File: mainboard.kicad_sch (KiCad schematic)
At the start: 86 parts, among them J1 Conn 02x05 1.27mm, J2 Conn 01x10 1.27mm, J3 Conn 02x10 1.27mm, J4 Conn +Z 02x05 2.00 mm, J5 Conn -Z 02x05 2.00 mm, J6 Conn +X 02x05 2.00 mm, J7 Conn -X 02x05 2.00 mm, J8 U.FL-R-SMT-1, J9 USB_C_Receptacle_USB2.0, SW1 KMR231NG, SW2 SW_SPDT, U1 ATSAMD51J20A-M, U10 USBLC6-2SC6, U2 MAX706RESA+, U3 AP2112K-3.3, U4 MR25H40, U5 BMX160, U6 RFM98PW, U7 DRV8830DRC, U8 DRV8830DRC, U9 DRV8830DRC, Y1 32.768kHz

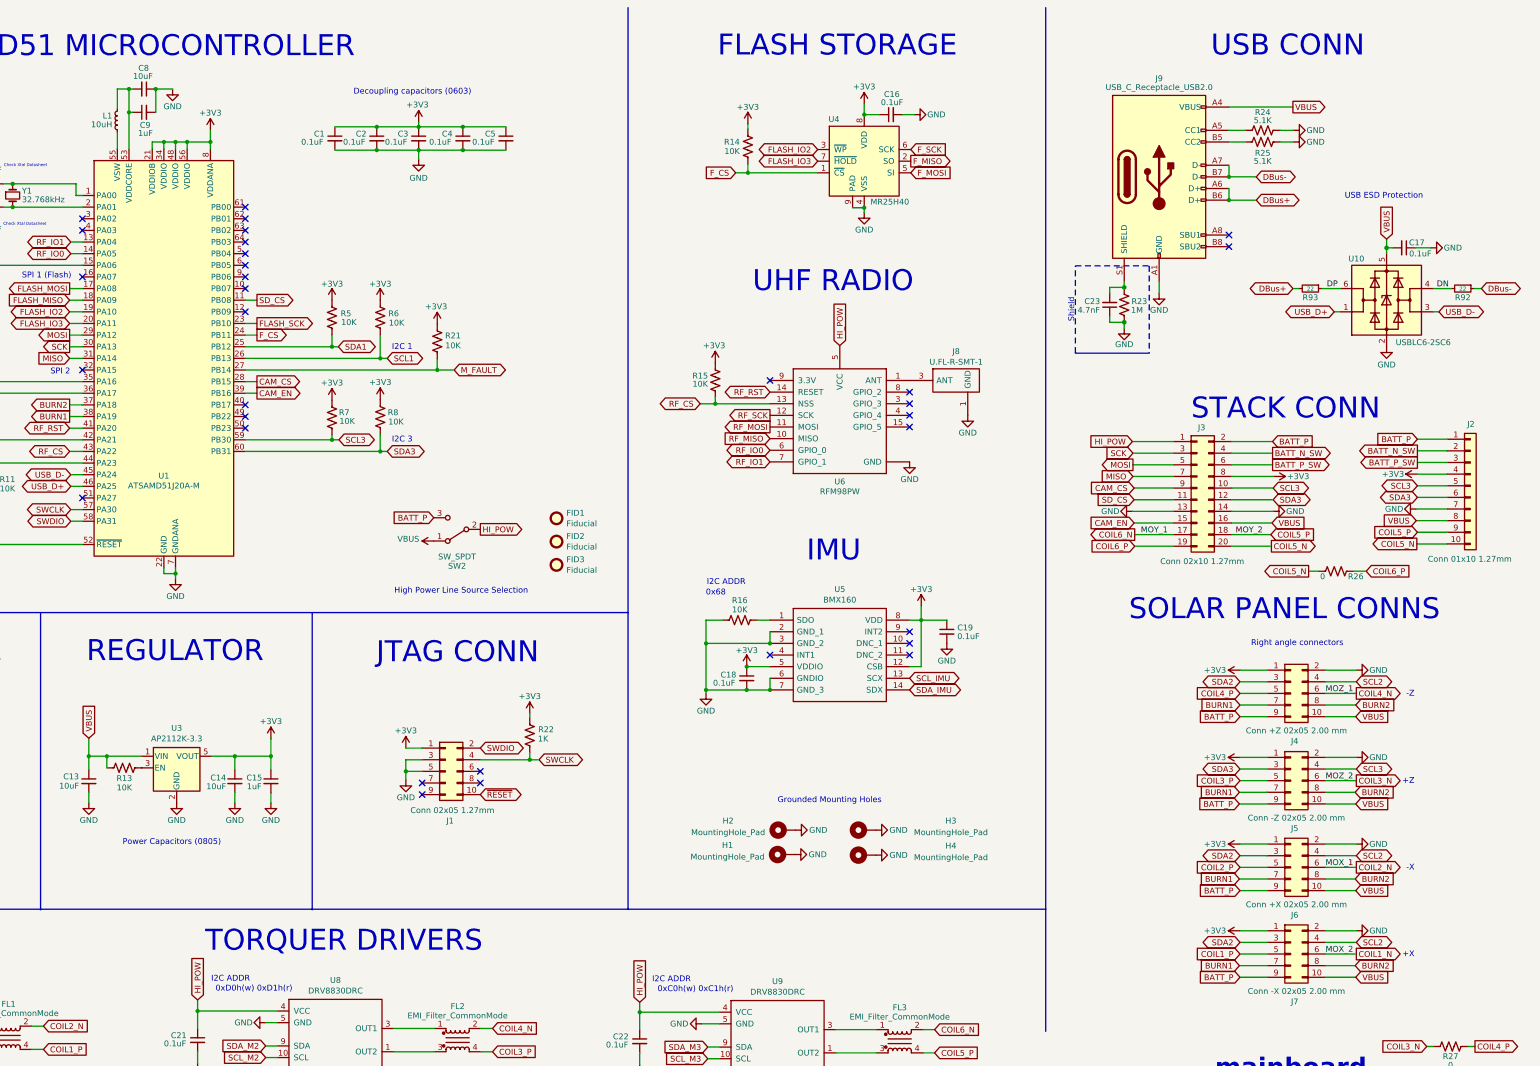
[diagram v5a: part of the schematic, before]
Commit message: added pulldown and 0 ohm resistor to VBUS. Renamed VBUS to VUSB
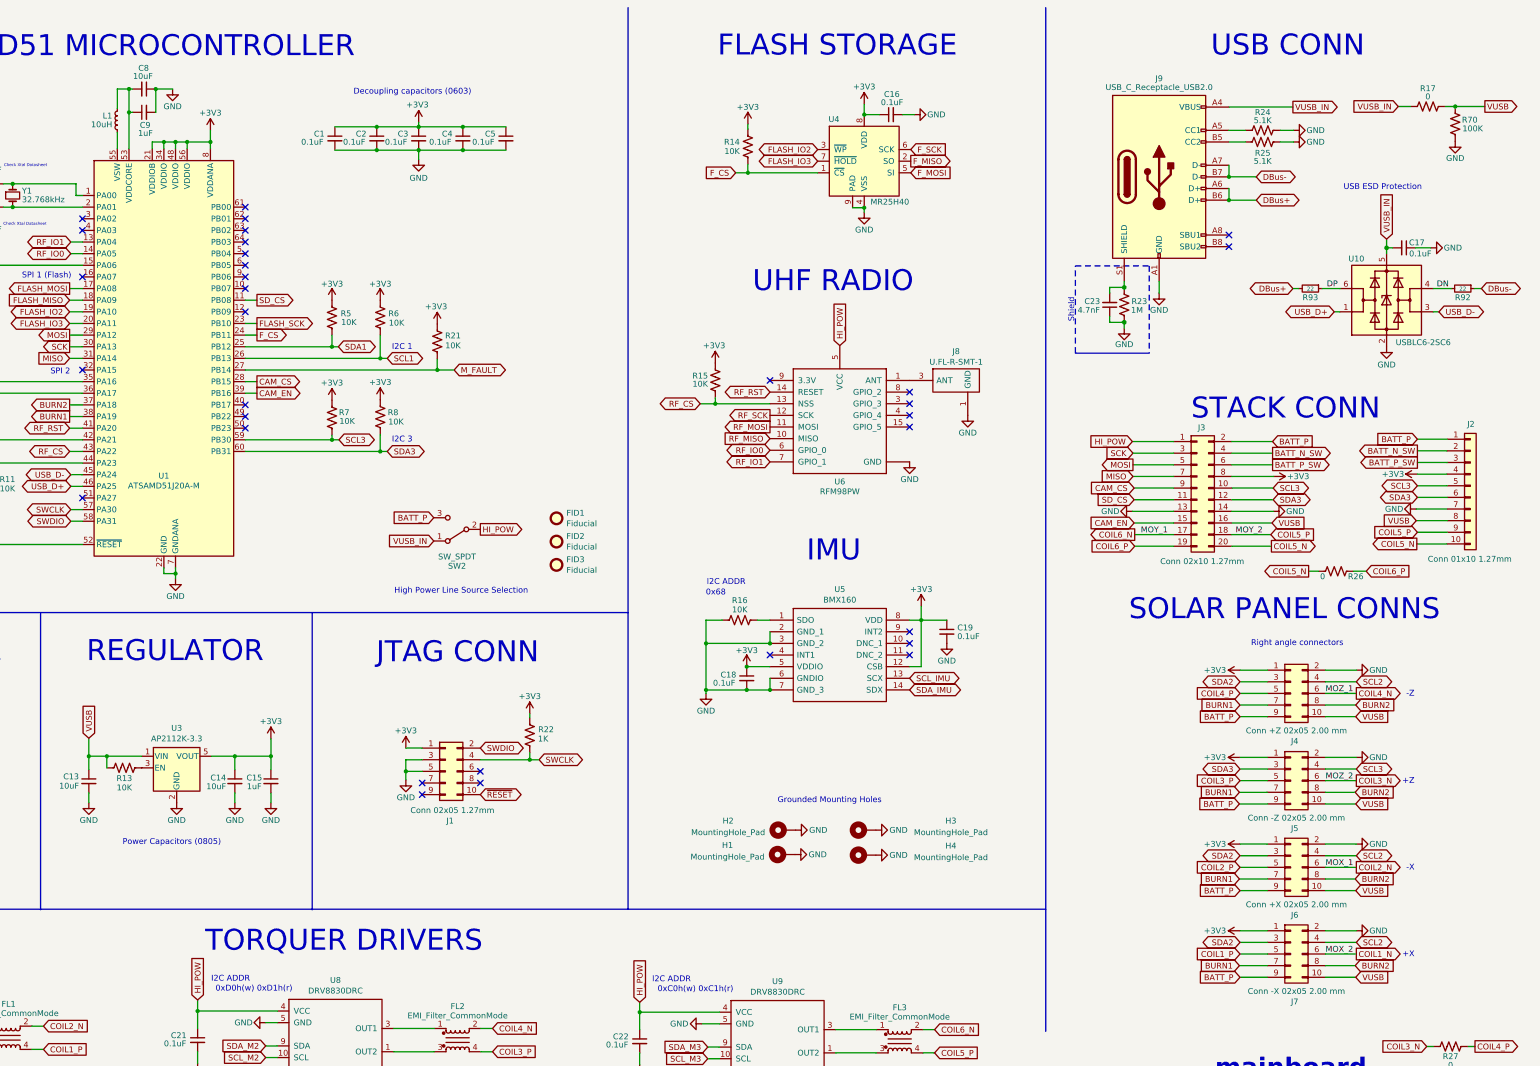
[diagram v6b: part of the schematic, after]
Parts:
- added R17: 0, Resistor_SMD:R_0603_1608Metric, symbol Device:R_US
- added R70: 100K, Resistor_SMD:R_0603_1608Metric, symbol Device:R_US
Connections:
- net GND: now also R70.2
- net VBUS renamed VUSB
- net VUSB: now also R17.2, R70.1; no longer C17.2, J9.A4 (VBUS), J9.A9 (VBUS), J9.B4 (VBUS), J9.B9 (VBUS), SW2.1 (A), U10.5 (VBUS)
- new net VUSB_IN: C17.2, J9.A4 (VBUS), J9.A9 (VBUS), J9.B4 (VBUS), J9.B9 (VBUS), R17.1, SW2.1 (A), U10.5 (VBUS)
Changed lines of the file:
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@@
   (junction (at 56.261 129.159) (diameter 0) (color 0 0 0 0)
   )
+  (junction (at 401.32 33.528) (diameter 0) (color 0 0 0 0)
+  )
   (junction (at 329.057 73.025) (diameter 1.016) (color 0 0 0 0)
   )
@@
     (stroke (width 0) (type default) (color 0 0 0 0))
   )
+  (wire (pts (xy 401.32 33.528) (xy 407.797 33.528))
+    (stroke (width 0) (type default) (color 0 0 0 0))
+  )
   (wire (pts (xy 144.145 233.553) (xy 141.605 233.553))
     (stroke (width 0) (type default) (color 0 0 0 0))
@@
     (stroke (width 0) (type default) (color 0 0 0 0))
   )
+  (wire (pts (xy 388.874 33.528) (xy 391.541 33.528))
+    (stroke (width 0) (type default) (color 0 0 0 0))
+  )
   (wire (pts (xy 139.7 96.139) (xy 137.16 96.139))
     (stroke (width 0) (type default) (color 0 0 0 0))
@@
     (stroke (width 0) (type default) (color 0 0 0 0))
   )
+  (wire (pts (xy 401.32 33.528) (xy 399.161 33.528))
+    (stroke (width 0) (type default) (color 0 0 0 0))
+  )
   (wire (pts (xy 46.101 248.285) (xy 43.561 248.285))
     (stroke (width 0) (type default) (color 0 0 0 0))
@@
     (effects (font (size 1.27 1.27)) (justify right bottom))
   )
-  (text "USB ESD Protection" (at 377.19 53.848 0)
+  (text "USB ESD Protection" (at 376.936 51.943 0)
     (effects (font (size 1.27 1.27)) (justify left bottom))
   )
@@
     )
   )
-  (global_label "VBUS" (shape input) (at 102.997 171.45 90) (fields_autoplaced)
+  (global_label "VUSB" (shape input) (at 102.997 171.45 90) (fields_autoplaced)
     (effects (font (size 1.27 1.27)) (justify left))
     (property "Intersheet References" "${INTERSHEET_REFS}" (id 0) (at 102.9176 164.2272 90)
@@
     )
   )
+  (global_label "VUSB_IN" (shape input) (at 388.874 33.528 180) (fields_autoplaced)
+    (effects (font (size 1.27 1.27)) (justify right))
+    (property "Intersheet References" "${INTERSHEET_REFS}" (id 0) (at 378.7484 33.6074 0)
+      (effects (font (size 1.27 1.27)) (justify right) hide)
+    )
+  )
   (global_label "DBus-" (shape bidirectional) (at 357.886 48.895 0) (fields_autoplaced)
     (effects (font (size 1.27 1.27)) (justify left))
@@
     )
   )
-  (global_label "VBUS" (shape input) (at 379.603 185.801 0) (fields_autoplaced)
+  (global_label "VUSB" (shape input) (at 379.603 185.801 0) (fields_autoplaced)
     (effects (font (size 1.27 1.27)) (justify left))
     (property "Intersheet References" "${INTERSHEET_REFS}" (id 0) (at 386.8258 185.7216 0)
@@
     )
   )
-  (global_label "VBUS" (shape input) (at 392.811 123.952 180) (fields_autoplaced)
+  (global_label "VUSB" (shape input) (at 392.811 123.952 180) (fields_autoplaced)
     (effects (font (size 1.27 1.27)) (justify right))
     (property "Intersheet References" "${INTERSHEET_REFS}" (id 0) (at 385.5882 124.0314 0)
@@
     )
   )
+  (global_label "VUSB" (shape output) (at 407.797 33.528 0) (fields_autoplaced)
+    (effects (font (size 1.27 1.27)) (justify left))
+    (property "Intersheet References" "${INTERSHEET_REFS}" (id 0) (at 415.0198 33.4486 0)
+      (effects (font (size 1.27 1.27)) (justify left) hide)
+    )
+  )
   (global_label "COIL6_P" (shape input) (at 331.343 129.54 180) (fields_autoplaced)
     (effects (font (size 1.27 1.27)) (justify right))
@@
     )
   )
+  (global_label "VUSB_IN" (shape input) (at 178.308 128.397 180) (fields_autoplaced)
+    (effects (font (size 1.27 1.27)) (justify right))
+    (property "Intersheet References" "${INTERSHEET_REFS}" (id 0) (at 168.1824 128.4764 0)
+      (effects (font (size 1.27 1.27)) (justify right) hide)
+    )
+  )
   (global_label "COIL5_P" (shape input) (at 287.655 240.157 0) (fields_autoplaced)
     (effects (font (size 1.27 1.27)) (justify left))
@@
     )
   )
-  (global_label "VBUS" (shape output) (at 365.887 33.655 0) (fields_autoplaced)
+  (global_label "VUSB_IN" (shape output) (at 365.887 33.655 0) (fields_autoplaced)
     (effects (font (size 1.27 1.27)) (justify left))
-    (property "Intersheet References" "${INTERSHEET_REFS}" (id 0) (at 373.1098 33.5756 0)
+    (property "Intersheet References" "${INTERSHEET_REFS}" (id 0) (at 376.0126 33.5756 0)
       (effects (font (size 1.27 1.27)) (justify left) hide)
     )
@@
     )
   )
-  (global_label "VBUS" (shape input) (at 379.603 223.647 0) (fields_autoplaced)
+  (global_label "VUSB" (shape input) (at 379.603 223.647 0) (fields_autoplaced)
     (effects (font (size 1.27 1.27)) (justify left))
     (property "Intersheet References" "${INTERSHEET_REFS}" (id 0) (at 386.8258 223.5676 0)
@@
     )
   )
-  (global_label "VBUS" (shape input) (at 379.603 166.751 0) (fields_autoplaced)
+  (global_label "VUSB" (shape input) (at 379.603 166.751 0) (fields_autoplaced)
     (effects (font (size 1.27 1.27)) (justify left))
     (property "Intersheet References" "${INTERSHEET_REFS}" (id 0) (at 386.8258 166.6716 0)
@@
     )
   )
-  (global_label "VBUS" (shape input) (at 379.603 204.724 0) (fields_autoplaced)
+  (global_label "VUSB" (shape input) (at 379.603 204.724 0) (fields_autoplaced)
     (effects (font (size 1.27 1.27)) (justify left))
     (property "Intersheet References" "${INTERSHEET_REFS}" (id 0) (at 386.8258 204.6446 0)
@@
     )
   )
-  (global_label "VBUS" (shape input) (at 361.315 124.46 0) (fields_autoplaced)
+  (global_label "VUSB" (shape input) (at 361.315 124.46 0) (fields_autoplaced)
     (effects (font (size 1.27 1.27)) (justify left))
     (property "Intersheet References" "${INTERSHEET_REFS}" (id 0) (at 368.5378 124.5394 0)
@@
     )
   )
-  (global_label "VBUS" (shape input) (at 386.334 62.484 90) (fields_autoplaced)
+  (global_label "VUSB_IN" (shape input) (at 386.334 62.484 90) (fields_autoplaced)
     (effects (font (size 1.27 1.27)) (justify left))
-    (property "Intersheet References" "${INTERSHEET_REFS}" (id 0) (at 386.2546 55.2612 90)
+    (property "Intersheet References" "${INTERSHEET_REFS}" (id 0) (at 386.2546 52.3584 90)
       (effects (font (size 1.27 1.27)) (justify left) hide)
     )
@@
     (pin "2")
   )
+  (symbol (lib_id "Device:R_US") (at 395.351 33.528 90) (unit 1)
+    (in_bom yes) (on_board yes)
+    (property "Reference" "R17" (id 0) (at 395.351 29.591 90))
+    (property "Value" "0" (id 1) (at 395.351 31.369 90))
+    (property "Footprint" "Resistor_SMD:R_0603_1608Metric" (id 2) (at 395.605 32.512 90)
+      (effects (font (size 1.27 1.27)) hide)
+    )
+    (property "Datasheet" "~" (id 3) (at 395.351 33.528 0)
+      (effects (font (size 1.27 1.27)) hide)
+    )
+    (pin "1")
+    (pin "2")
+  )
   (symbol (lib_id "power:GND") (at 274.828 191.516 90) (unit 1)
     (in_bom yes) (on_board yes)
@@
     (pin "2")
   )
+  (symbol (lib_id "Device:R_US") (at 401.32 37.338 0) (unit 1)
+    (in_bom yes) (on_board yes)
+    (property "Reference" "R70" (id 0) (at 404.495 36.449 0))
+    (property "Value" "100K" (id 1) (at 405.13 38.354 0))
+    (property "Footprint" "Resistor_SMD:R_0603_1608Metric" (id 2) (at 402.336 37.592 90)
+      (effects (font (size 1.27 1.27)) hide)
+    )
+    (property "Datasheet" "~" (id 3) (at 401.32 37.338 0)
+      (effects (font (size 1.27 1.27)) hide)
+    )
+    (pin "1")
+    (pin "2")
+  )
   (symbol (lib_id "power:GND") (at 395.986 64.389 90) (unit 1)
     (in_bom yes) (on_board yes)
@@
     (pin "1")
   )
+  (symbol (lib_id "power:GND") (at 401.32 41.148 0) (unit 1)
+    (in_bom yes) (on_board yes)
+    (property "Reference" "#PWR0124" (id 0) (at 401.32 47.498 0)
+      (effects (font (size 1.27 1.27)) hide)
+    )
+    (property "Value" "GND" (id 1) (at 401.32 44.831 0))
+    (property "Footprint" "" (id 2) (at 401.32 41.148 0)
+      (effects (font (size 1.27 1.27)) hide)
+    )
+    (property "Datasheet" "" (id 3) (at 401.32 41.148 0)
+      (effects (font (size 1.27 1.27)) hide)
+    )
+    (pin "1")
+  )
   (symbol (lib_id "power:GND") (at 329.057 81.915 0) (unit 1)
     (in_bom yes) (on_board yes)
@@
     (pin "2")
   )
-  (symbol (lib_id "power:VBUS") (at 178.308 128.397 90) (unit 1)
-    (in_bom yes) (on_board yes) (fields_autoplaced)
-    (property "Reference" "#PWR0112" (id 0) (at 182.118 128.397 0)
-      (effects (font (size 1.27 1.27)) hide)
-    )
-    (property "Value" "VBUS" (id 1) (at 175.133 127.9632 90)
-      (effects (font (size 1.27 1.27)) (justify left))
-    )
-    (property "Footprint" "" (id 2) (at 178.308 128.397 0)
-      (effects (font (size 1.27 1.27)) hide)
-    )
-    (property "Datasheet" "" (id 3) (at 178.308 128.397 0)
-      (effects (font (size 1.27 1.27)) hide)
-    )
-    (pin "1")
-  )
   (symbol (lib_id "Device:C_Small") (at 175.006 40.513 0) (unit 1)
     (in_bom yes) (on_board yes)
@@
       (reference "#PWR0111") (unit 1) (value "GND") (footprint "")
     )
-    (path "/dace08e9-2794-4eeb-968a-8ff63b4b9f51"
-      (reference "#PWR0112") (unit 1) (value "VBUS") (footprint "")
-    )
     (path "/2e088d9c-4345-4234-9fbc-b28bd25e7d74"
       (reference "#PWR0113") (unit 1) (value "+3V3") (footprint "")
@@
       (reference "#PWR0123") (unit 1) (value "GND") (footprint "")
     )
+    (path "/50e5377b-5519-48e6-ba4e-974f66fffe95"
+      (reference "#PWR0124") (unit 1) (value "GND") (footprint "")
+    )
     (path "/cd60d17a-4ffb-4042-a426-fdeb8e7d577a"
       (reference "#PWR0126") (unit 1) (value "+3V3") (footprint "")
@@
       (reference "R16") (unit 1) (value "10K") (footprint "Resistor_SMD:R_0603_1608Metric")
     )
+    (path "/1d7e6e2e-67a0-4278-a837-5da214f06a1e"
+      (reference "R17") (unit 1) (value "0") (footprint "Resistor_SMD:R_0603_1608Metric")
+    )
     (path "/00000000-0000-0000-0000-00005e74913a"
       (reference "R18") (unit 1) (value "0") (footprint "Resistor_SMD:R_0603_1608Metric")
@@
       (reference "R69") (unit 1) (value "0") (footprint "Resistor_SMD:R_0603_1608Metric")
     )
+    (path "/44714030-b74c-47b1-8cdb-296d3c08673a"
+      (reference "R70") (unit 1) (value "100K") (footprint "Resistor_SMD:R_0603_1608Metric")
+    )
     (path "/89e9ad27-deb2-49f4-bcf8-1a7a63ce9e3a/d08973d1-a9aa-4e3b-a55a-a663d36864d8"

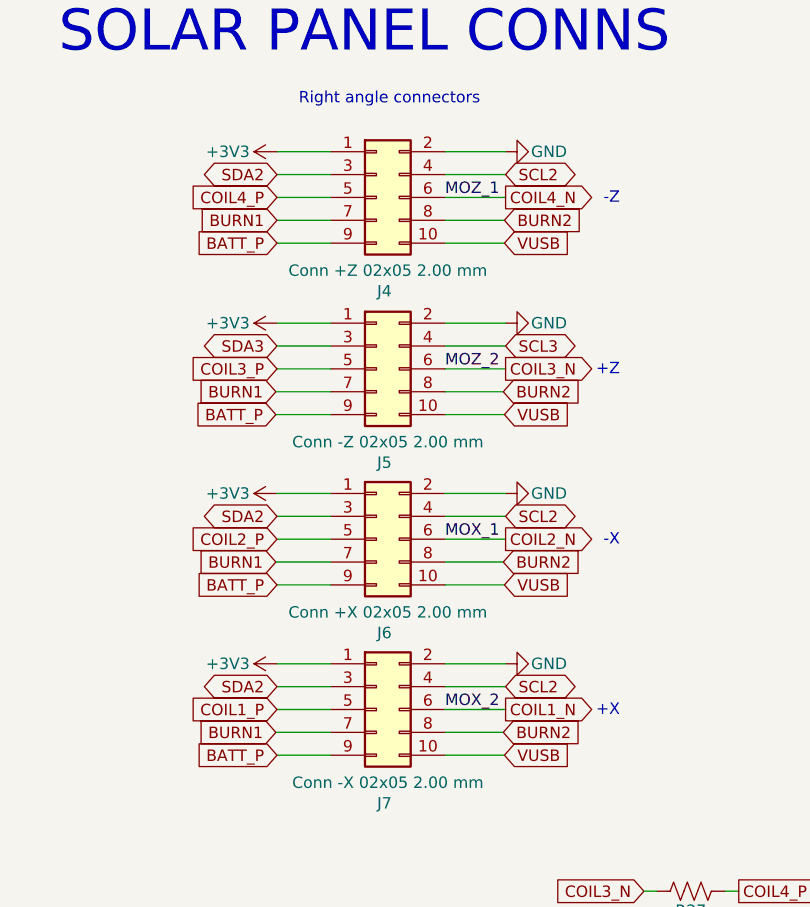
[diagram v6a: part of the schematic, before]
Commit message: Updated Mainboard-Solar Panels X/Z Connectors
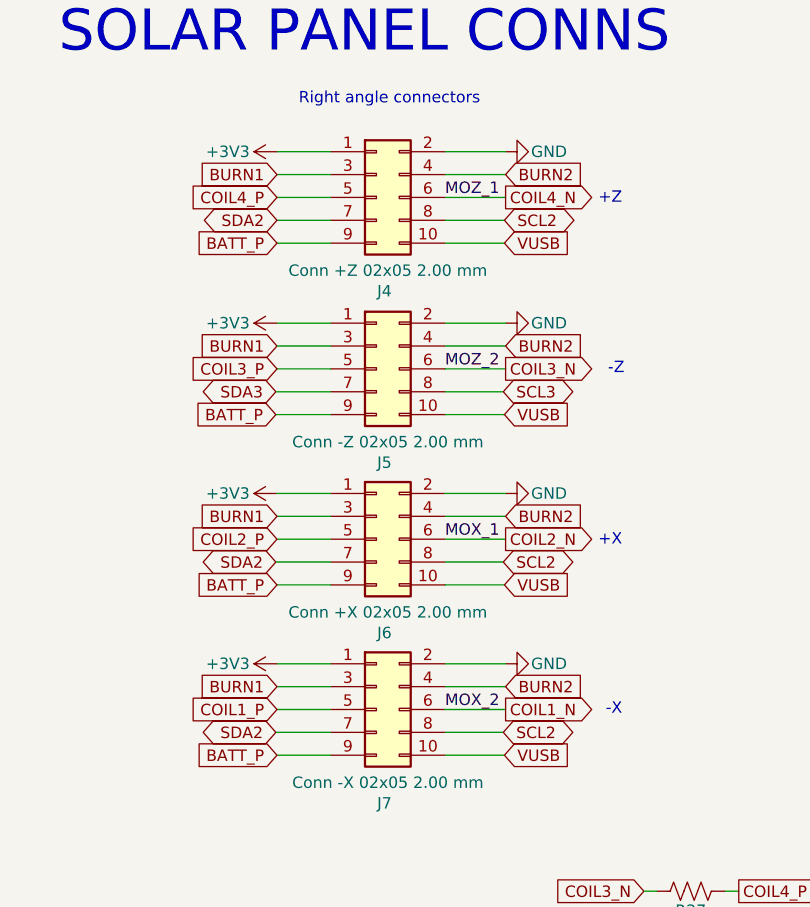
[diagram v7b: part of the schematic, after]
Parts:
- J4, J5, J6, J7: footprint mainboard:15250102601000 -> mainboard:SAMTEC_SFMH-105-02-L-D-WT
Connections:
- net BURN1: now also J4.3 (Pin_3), J5.3 (Pin_3), J6.3 (Pin_3), J7.3 (Pin_3); no longer J4.7 (Pin_7), J5.7 (Pin_7), J6.7 (Pin_7), J7.7 (Pin_7)
- net BURN2: now also J4.4 (Pin_4), J5.4 (Pin_4), J6.4 (Pin_4), J7.4 (Pin_4); no longer J4.8 (Pin_8), J5.8 (Pin_8), J6.8 (Pin_8), J7.8 (Pin_8)
- net SCL2: now also J4.8 (Pin_8), J6.8 (Pin_8), J7.8 (Pin_8); no longer J4.4 (Pin_4), J6.4 (Pin_4), J7.4 (Pin_4)
- net SCL3: now also J5.8 (Pin_8); no longer J5.4 (Pin_4)
- net SDA2: now also J4.7 (Pin_7), J6.7 (Pin_7), J7.7 (Pin_7); no longer J4.3 (Pin_3), J6.3 (Pin_3), J7.3 (Pin_3)
- net SDA3: now also J5.7 (Pin_7); no longer J5.3 (Pin_3)
